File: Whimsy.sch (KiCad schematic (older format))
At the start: 3 parts, among them J1 OLED, J2 LED Breakout, U1 Elite-C

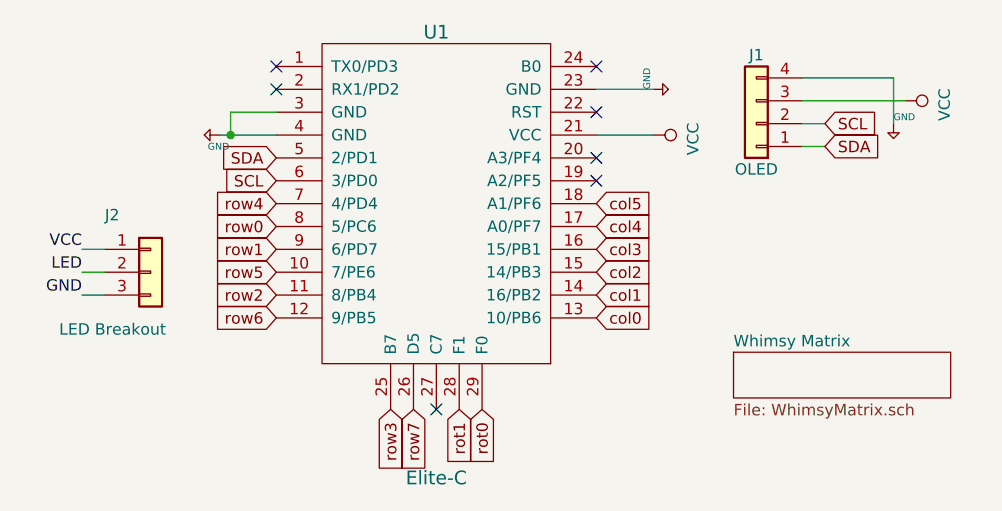
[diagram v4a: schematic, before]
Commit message: gnd pins were not working as inteded, solder mask was a little off, fixed overall matrix, tightened the schematic to make it more logical
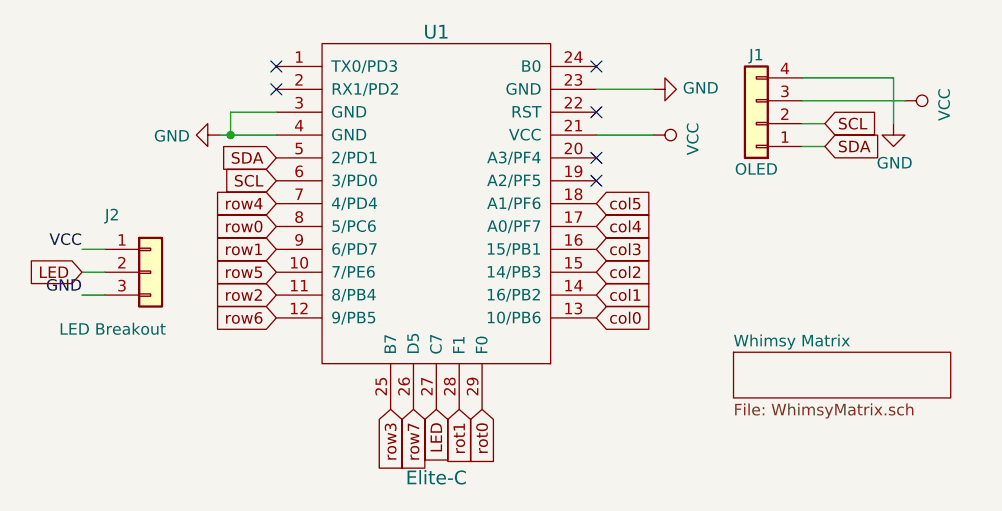
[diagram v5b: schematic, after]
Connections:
- net +5V is gone; now on net GND: J1.4 (Pin_4), U1.23 (GND), U1.3 (GND), U1.4 (GND)
- net LED: now also U1.27 (C7)
- no-connect marks 7 -> 6
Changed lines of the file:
@@
 $EndBitmap
-$Comp
-L keyboard_parts:GND #PWR0102
-U 1 1 5E67912E
-P 6400 3600
-F 0 "#PWR0102" H 6400 3650 20  0001 C CNN
-F 1 "GND" H 6400 3629 30  0000 L CNN
-F 2 "" H 6400 3600 60  0000 C CNN
-F 3 "" H 6400 3600 60  0000 C CNN
-	1    6400 3600
-	1    0    0    -1
-$EndComp
 $Comp
 L power:VCC #PWR0103
@@
 	6000 3600 6100 3600
 $Comp
-L keyboard_parts:GND #PWR0104
-U 1 1 5E6ABEA3
-P 3450 3650
-F 0 "#PWR0104" H 3450 3700 20  0001 C CNN
-F 1 "GND" V 3500 3600 30  0000 L CNN
-F 2 "" H 3450 3650 60  0000 C CNN
-F 3 "" H 3450 3650 60  0000 C CNN
-	1    3450 3650
-	0    1    1    0
-$EndComp
-$Comp
 L power:VCC #PWR0105
 U 1 1 5E6AEA7D
@@
 	1    5350 3650
 	0    1    1    0
-$EndComp
-$Comp
-L keyboard_parts:GND #PWR0106
-U 1 1 5E6AF358
-P 5350 3450
-F 0 "#PWR0106" H 5350 3500 20  0001 C CNN
-F 1 "GND" H 5350 3479 30  0000 L CNN
-F 2 "" H 5350 3450 60  0000 C CNN
-F 3 "" H 5350 3450 60  0000 C CNN
-	1    5350 3450
-	0    -1   -1   0
 $EndComp
 Text GLabel 6100 3700 2    50   Input ~ 0
@@
 Text Label 2850 4350 2    50   ~ 0
 GND
-Text Label 2850 4250 2    50   ~ 0
-LED
 Wire Wire Line
 	2850 4150 2950 4150
@@
 NoConn ~ 3700 3450
 NoConn ~ 3700 3350
-NoConn ~ 4400 4850
 NoConn ~ 5100 3550
+Text GLabel 2850 4250 0    50   Input ~ 0
+LED
+Text GLabel 4400 4850 3    50   Input ~ 0
+LED
+$Comp
+L power:GND #PWR0101
+U 1 1 5E65D345
+P 3450 3650
+F 0 "#PWR0101" H 3450 3400 50  0001 C CNN
+F 1 "GND" V 3455 3522 50  0000 R CNN
+F 2 "" H 3450 3650 50  0001 C CNN
+F 3 "" H 3450 3650 50  0001 C CNN
+	1    3450 3650
+	0    1    1    0
+$EndComp
+$Comp
+L power:GND #PWR0102
+U 1 1 5E65D9B0
+P 5350 3450
+F 0 "#PWR0102" H 5350 3200 50  0001 C CNN
+F 1 "GND" V 5355 3322 50  0000 R CNN
+F 2 "" H 5350 3450 50  0001 C CNN
+F 3 "" H 5350 3450 50  0001 C CNN
+	1    5350 3450
+	0    -1   -1   0
+$EndComp
+$Comp
+L power:GND #PWR0104
+U 1 1 5E65E8A7
+P 6400 3600
+F 0 "#PWR0104" H 6400 3350 50  0001 C CNN
+F 1 "GND" H 6405 3427 50  0000 C CNN
+F 2 "" H 6400 3600 50  0001 C CNN
+F 3 "" H 6400 3600 50  0001 C CNN
+	1    6400 3600
+	1    0    0    -1
+$EndComp
 $EndSCHEMATC

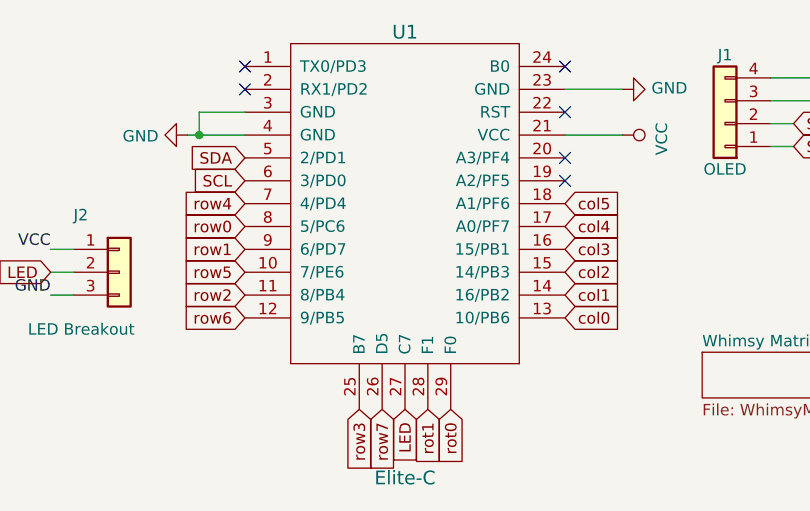
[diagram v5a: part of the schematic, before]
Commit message: flipped the elite-c, re-routed a lot of the board, tidied up some traces, new render, updated readme
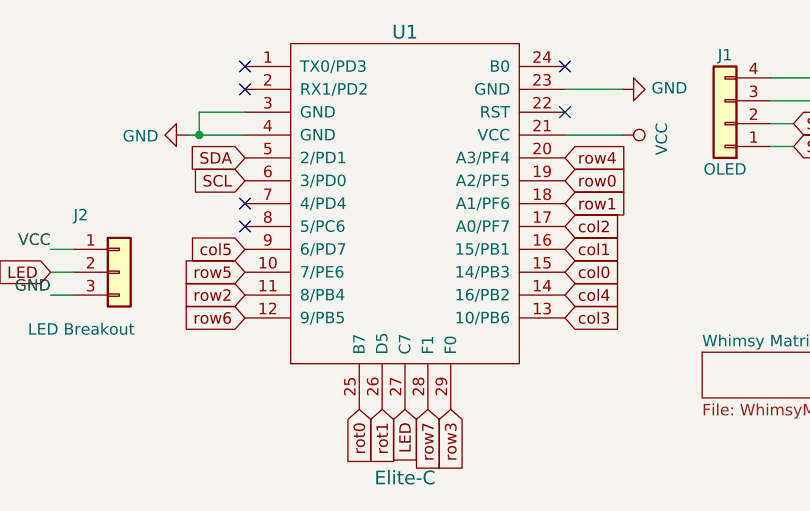
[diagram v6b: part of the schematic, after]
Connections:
- net col0: now also U1.15 (14/PB3); no longer U1.13 (10/PB6)
- net col1: now also U1.16 (15/PB1); no longer U1.14 (16/PB2)
- net col2: now also U1.17 (A0/PF7); no longer U1.15 (14/PB3)
- net col3: now also U1.13 (10/PB6); no longer U1.16 (15/PB1)
- net col4: now also U1.14 (16/PB2); no longer U1.17 (A0/PF7)
- net col5: now also U1.9 (6/PD7); no longer U1.18 (A1/PF6)
- net rot0: now also U1.25 (B7); no longer U1.29 (F0)
- net rot1: now also U1.26 (D5); no longer U1.28 (F1)
- net row0: now also U1.19 (A2/PF5); no longer U1.8 (5/PC6)
- net row1: now also U1.18 (A1/PF6); no longer U1.9 (6/PD7)
- net row3: now also U1.29 (F0); no longer U1.25 (B7)
- net row4: now also U1.20 (A3/PF4); no longer U1.7 (4/PD4)
- net row7: now also U1.28 (F1); no longer U1.26 (D5)
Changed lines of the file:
@@
 Text GLabel 3700 3850 0    50   Input ~ 0
 SCL
+Text GLabel 5100 4250 2    50   Input ~ 0
+col0
+Text GLabel 5100 4150 2    50   Input ~ 0
+col1
+Text GLabel 5100 4050 2    50   Input ~ 0
+col2
 Text GLabel 5100 4450 2    50   Input ~ 0
-col0
-Text GLabel 5100 4350 2    50   Input ~ 0
-col1
-Text GLabel 5100 4250 2    50   Input ~ 0
-col2
-Text GLabel 5100 4150 2    50   Input ~ 0
 col3
-Text GLabel 3700 4050 0    50   Input ~ 0
+Text GLabel 5100 3850 2    50   Input ~ 0
 row0
-Text GLabel 3700 4150 0    50   Input ~ 0
+Text GLabel 5100 3950 2    50   Input ~ 0
 row1
 Text GLabel 3700 4350 0    50   Input ~ 0
 row2
-Text GLabel 4200 4850 3    50   Input ~ 0
+Text GLabel 4600 4850 3    50   Input ~ 0
 row3
-Text GLabel 3700 3950 0    50   Input ~ 0
+Text GLabel 5100 3750 2    50   Input ~ 0
 row4
 Text GLabel 3700 4250 0    50   Input ~ 0
@@
 Text GLabel 3700 4450 0    50   Input ~ 0
 row6
-Text GLabel 4300 4850 3    50   Input ~ 0
+Text GLabel 4500 4850 3    50   Input ~ 0
 row7
-Text GLabel 5100 4050 2    50   Input ~ 0
+Text GLabel 5100 4350 2    50   Input ~ 0
 col4
-Text GLabel 5100 3950 2    50   Input ~ 0
+Text GLabel 3700 4150 0    50   Input ~ 0
 col5
 $Comp
@@
 Wire Wire Line
 	2950 4350 2850 4350
-Text GLabel 4600 4850 3    50   Input ~ 0
+Text GLabel 4200 4850 3    50   Input ~ 0
 rot0
-Text GLabel 4500 4850 3    50   Input ~ 0
+Text GLabel 4300 4850 3    50   Input ~ 0
 rot1
 $Comp
@@
 Wire Wire Line
 	5100 3650 5350 3650
-NoConn ~ 5100 3850
-NoConn ~ 5100 3750
+NoConn ~ 3700 4050
+NoConn ~ 3700 3950
 NoConn ~ 5100 3350
 NoConn ~ 3700 3450
